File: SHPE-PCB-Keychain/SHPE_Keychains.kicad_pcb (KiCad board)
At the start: 2 copper layers, 14 x 12 mm, 4 parts, among them J1 USB_A

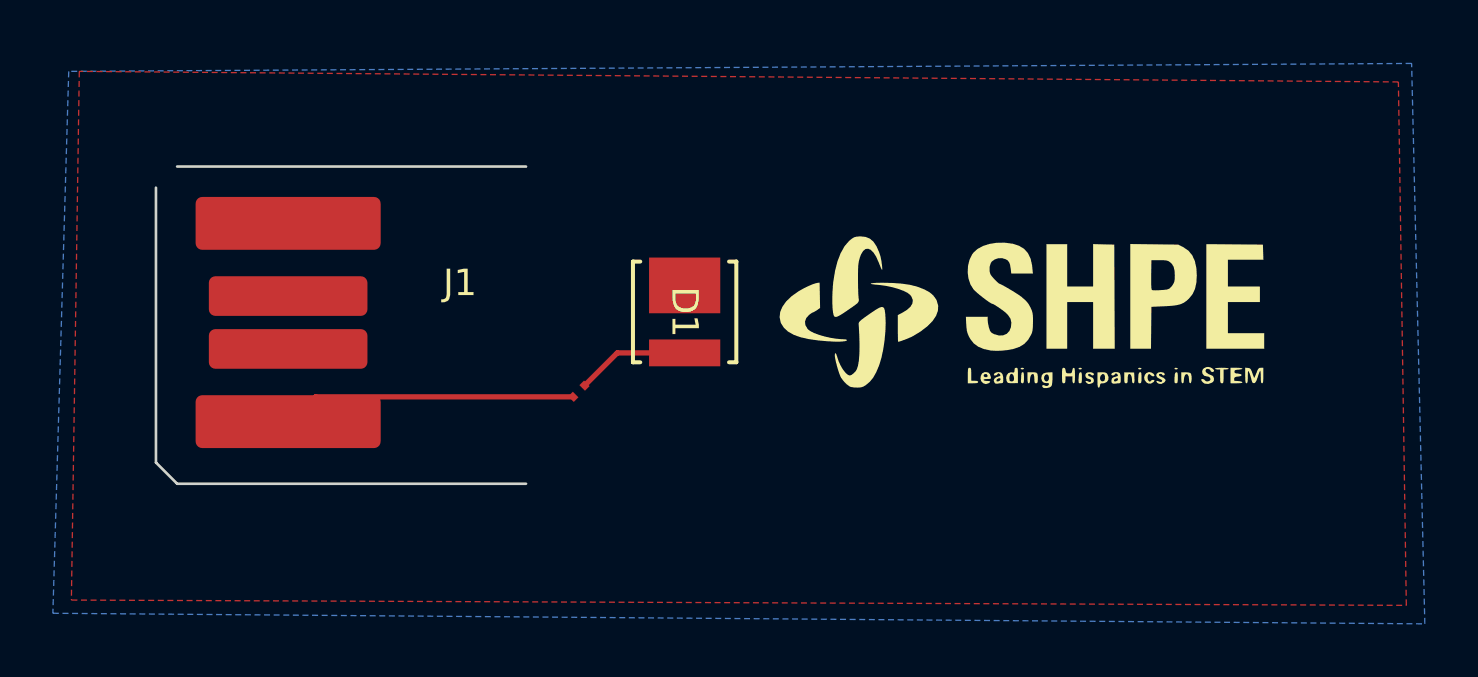
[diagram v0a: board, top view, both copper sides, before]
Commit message: added footprint folder
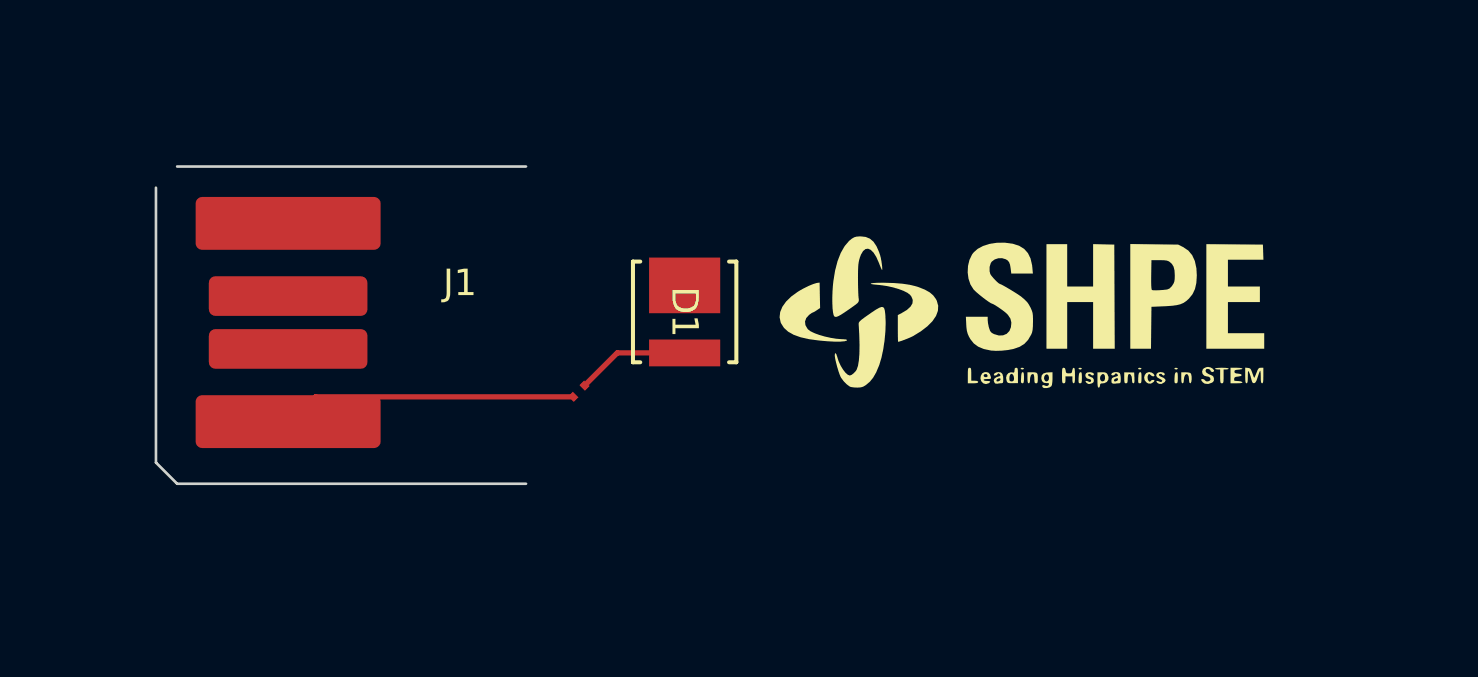
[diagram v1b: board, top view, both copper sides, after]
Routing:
- removed copper zone on B.Cu, net (none)
- removed copper zone on F.Cu, net (none)
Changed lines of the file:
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@@
 		(net 3)
-	)
-	(zone
-		(net 0)
-		(net_name "")
-		(layer "F.Cu")
-		(hatch edge 0.5)
-		(connect_pads
-			(clearance 0.5)
-		)
-		(min_thickness 0.25)
-		(filled_areas_thickness no)
-		(fill yes
-			(thermal_gap 0.5)
-			(thermal_bridge_width 0.5)
-			(island_removal_mode 1)
-			(island_area_min 10)
-		)
-		(polygon
-			(pts
-				(xy 120.1 49.9) (xy 119.8 69.9) (xy 170.3 70.1) (xy 170 50.3)
-			)
-		)
-	)
-	(zone
-		(net 0)
-		(net_name "")
-		(layer "B.Cu")
-		(hatch edge 0.5)
-		(priority 1)
-		(connect_pads
-			(clearance 0.5)
-		)
-		(min_thickness 0.25)
-		(filled_areas_thickness no)
-		(fill yes
-			(thermal_gap 0.5)
-			(thermal_bridge_width 0.5)
-			(island_removal_mode 1)
-			(island_area_min 10)
-		)
-		(polygon
-			(pts
-				(xy 119.7 49.9) (xy 119.1 70.4) (xy 171 70.8) (xy 170.5 49.6)
-			)
-		)
 	)
 	(embedded_fonts no)

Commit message: made changes to PCB
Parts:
- added G***: LOGO, LOGO, B.Cu at (151.1, 58.6)
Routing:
- net GND: vias 0 -> 7
- added copper zone on B.Cu, net (none)
- added copper zone on F.Cu, net GND
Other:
- board size 14 x 12 mm -> 44 x 15 mm
